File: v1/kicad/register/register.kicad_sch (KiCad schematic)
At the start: 5 parts, among them J1 DBUS, J2 BASE, J3 CTRL, U1 74LS173, U2 74LS173

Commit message: progress on kicad implementation
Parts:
- removed J1: DBUS, Connector_PinSocket_2.54mm:PinSocket_1x08_P2.54mm_Vertical, symbol Connector_Generic:Conn_01x08
- removed J2: BASE, Connector_PinSocket_2.54mm:PinSocket_1x04_P2.54mm_Vertical, symbol Connector_Generic:Conn_01x04
- removed J3: CTRL, Connector_PinHeader_2.54mm:PinHeader_1x03_P2.54mm_Vertical, symbol Connector_Generic:Conn_01x03
- removed U1, U2: 74LS173, Package_DIP:DIP-16_W7.62mm, symbol 74xx:74LS173
- added J1: RegisterSocket (active-high reset), LNCPU:RegisterPort, symbol LNCPU:RegisterSocket (active-high reset)
- added J2: RegisterCtrl, Connector_PinHeader_2.54mm:PinHeader_1x03_P2.54mm_Vertical, symbol LNCPU:RegisterCtrl
- added J3: ASYNC_{out}, Connector_PinSocket_2.54mm:PinSocket_1x08_P2.54mm_Vertical, symbol Connector_Generic:Conn_01x08
- added U1, U2: 74HC173, Package_DIP:DIP-16_W7.62mm_LongPads, symbol 74xx:74HC173
- added U3: 74LS244, Package_DIP:DIP-20_W7.62mm_LongPads, symbol 74xx:74LS244
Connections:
- new net: J1.1 (VCC), U1.16 (VCC), U2.16 (VCC), U3.20 (VCC)
- new net: J1.2 (RST), U1.15 (Mr), U2.15 (Mr)
- new net: J1.3 (CLK), U1.7 (Cp), U2.7 (Cp)
- new net: J1.4 (GND), U1.1 (Oe1), U1.2 (Oe2), U1.8 (GND), U2.1 (Oe1), U2.2 (Oe2), U2.8 (GND), U3.10 (GND)
- new net: J2.1 (~{EN}), U1.10 (E2), U2.10 (E2), U3.1 (OEa)
- new net: J2.2 (~{R_{in}}), U1.9 (E1), U2.9 (E1)
- new net: J2.3 (~{R_{out}}), U3.19 (OEb)
- new net ASYNC0: J3.1 (Pin_1), U1.3 (Q0), U3.2 (I0a)
- new net ASYNC1: J3.2 (Pin_2), U1.4 (Q1), U3.4 (I1a)
- new net ASYNC2: J3.3 (Pin_3), U1.5 (Q2), U3.6 (I2a)
- new net ASYNC3: J3.4 (Pin_4), U1.6 (Q3), U3.8 (I3a)
- new net ASYNC4: J3.5 (Pin_5), U2.3 (Q0), U3.11 (I0b)
- new net ASYNC5: J3.6 (Pin_6), U2.4 (Q1), U3.13 (I1b)
- new net ASYNC6: J3.7 (Pin_7), U2.5 (Q2), U3.15 (I2b)
- new net ASYNC7: J3.8 (Pin_8), U2.6 (Q3), U3.17 (I3b)
- new net DBUS0: J1.5 (DBUS0), U1.14 (D0), U3.18 (O0a)
- new net DBUS1: J1.6 (DBUS1), U1.13 (D1), U3.16 (O1a)
- new net DBUS2: J1.7 (DBUS2), U1.12 (D2), U3.14 (O2a)
- new net DBUS3: J1.8 (DBUS3), U1.11 (D3), U3.12 (O3a)
- new net DBUS4: J1.9 (DBUS4), U2.14 (D0), U3.9 (O0b)
- new net DBUS5: J1.10 (DBUS5), U2.13 (D1), U3.7 (O1b)
- new net DBUS6: J1.11 (DBUS6), U2.12 (D2), U3.5 (O2b)
- new net DBUS7: J1.12 (DBUS7), U2.11 (D3), U3.3 (O3b)

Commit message: feat: update KiCad files with new pin configurations and error handling improvements
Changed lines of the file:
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@@
 (kicad_sch
-	(version 20231120)
+	(version 20250114)
 	(generator "eeschema")
-	(generator_version "8.0")
+	(generator_version "9.0")
 	(paper "A4")
 	(junction
@@
 	(label "ASYNC1"
 		(at 185.42 31.75 0)
-		(fields_autoplaced yes)
 		(effects
 			(font
@@
 	(label "ASYNC7"
 		(at 121.92 36.83 180)
-		(fields_autoplaced yes)
 		(effects
 			(font
@@
 	(label "ASYNC2"
 		(at 185.42 34.29 0)
-		(fields_autoplaced yes)
 		(effects
 			(font
@@
 	(label "ASYNC4"
 		(at 185.42 39.37 0)
-		(fields_autoplaced yes)
 		(effects
 			(font
@@
 	(label "ASYNC5"
 		(at 185.42 41.91 0)
-		(fields_autoplaced yes)
 		(effects
 			(font
@@
 	(label "ASYNC4"
 		(at 151.13 118.11 0)
-		(fields_autoplaced yes)
 		(effects
 			(font
@@
 	(label "ASYNC3"
 		(at 153.67 118.11 0)
-		(fields_autoplaced yes)
 		(effects
 			(font
@@
 	(label "DBUS6"
 		(at 102.87 149.86 0)
-		(fields_autoplaced yes)
 		(effects
 			(font
@@
 	(label "DBUS7"
 		(at 100.33 147.32 0)
-		(fields_autoplaced yes)
 		(effects
 			(font
@@
 	(label "ASYNC0"
 		(at 123.19 92.71 180)
-		(fields_autoplaced yes)
 		(effects
 			(font
@@
 	(label "DBUS4"
 		(at 107.95 154.94 0)
-		(fields_autoplaced yes)
 		(effects
 			(font
@@
 	(label "DBUS7"
 		(at 68.58 36.83 0)
-		(fields_autoplaced yes)
 		(effects
 			(font
@@
 	(label "ASYNC6"
 		(at 121.92 34.29 180)
-		(fields_autoplaced yes)
 		(effects
 			(font
@@
 	(label "DBUS0"
 		(at 210.82 29.21 180)
-		(fields_autoplaced yes)
 		(effects
 			(font
@@
 	(label "DBUS[0..7]"
 		(at 64.77 24.13 0)
-		(fields_autoplaced yes)
 		(effects
 			(font
@@
 	(label "DBUS3"
 		(at 110.49 157.48 0)
-		(fields_autoplaced yes)
 		(effects
 			(font
@@
 	(label "DBUS1"
 		(at 67.31 95.25 0)
-		(fields_autoplaced yes)
 		(effects
 			(font
@@
 	(label "DBUS2"
 		(at 67.31 97.79 0)
-		(fields_autoplaced yes)
 		(effects
 			(font
@@
 	(label "ASYNC0"
 		(at 161.29 118.11 0)
-		(fields_autoplaced yes)
 		(effects
 			(font
@@
 	(label "DBUS3"
 		(at 210.82 36.83 180)
-		(fields_autoplaced yes)
 		(effects
 			(font
@@
 	(label "DBUS0"
 		(at 67.31 92.71 0)
-		(fields_autoplaced yes)
 		(effects
 			(font
@@
 	(label "ASYNC4"
 		(at 121.92 29.21 180)
-		(fields_autoplaced yes)
 		(effects
 			(font
@@
 	(label "DBUS6"
 		(at 68.58 34.29 0)
-		(fields_autoplaced yes)
 		(effects
 			(font
@@
 	(label "ASYNC6"
 		(at 185.42 44.45 0)
-		(fields_autoplaced yes)
 		(effects
 			(font
@@
 	(label "DBUS4"
 		(at 210.82 39.37 180)
-		(fields_autoplaced yes)
 		(effects
 			(font
@@
 	(label "DBUS2"
 		(at 113.03 160.02 0)
-		(fields_autoplaced yes)
 		(effects
 			(font
@@
 	(label "ASYNC[0..7]"
 		(at 125.73 24.13 180)
-		(fields_autoplaced yes)
 		(effects
 			(font
@@
 	(label "ASYNC3"
 		(at 123.19 100.33 180)
-		(fields_autoplaced yes)
 		(effects
 			(font
@@
 	(label "DBUS7"
 		(at 210.82 46.99 180)
-		(fields_autoplaced yes)
 		(effects
 			(font
@@
 	(label "ASYNC5"
 		(at 148.59 118.11 0)
-		(fields_autoplaced yes)
 		(effects
 			(font
@@
 	(label "ASYNC2"
 		(at 123.19 97.79 180)
-		(fields_autoplaced yes)
 		(effects
 			(font
@@
 	(label "DBUS5"
 		(at 68.58 31.75 0)
-		(fields_autoplaced yes)
 		(effects
 			(font
@@
 	(label "ASYNC0"
 		(at 185.42 29.21 0)
-		(fields_autoplaced yes)
 		(effects
 			(font
@@
 	(label "DBUS6"
 		(at 210.82 44.45 180)
-		(fields_autoplaced yes)
 		(effects
 			(font
@@
 	(label "ASYNC1"
 		(at 158.75 118.11 0)
-		(fields_autoplaced yes)
 		(effects
 			(font
@@
 	(label "DBUS1"
 		(at 210.82 31.75 180)
-		(fields_autoplaced yes)
 		(effects
 			(font
@@
 	(label "DBUS0"
 		(at 118.11 165.1 0)
-		(fields_autoplaced yes)
 		(effects
 			(font
@@
 	(label "DBUS3"
 		(at 67.31 100.33 0)
-		(fields_autoplaced yes)
 		(effects
 			(font
@@
 	(label "DBUS5"
 		(at 105.41 152.4 0)
-		(fields_autoplaced yes)
 		(effects
 			(font
@@
 	(label "ASYNC3"
 		(at 185.42 36.83 0)
-		(fields_autoplaced yes)
 		(effects
 			(font
@@
 	(label "DBUS2"
 		(at 210.82 34.29 180)
-		(fields_autoplaced yes)
 		(effects
 			(font
@@
 	(label "ASYNC7"
 		(at 143.51 118.11 0)
-		(fields_autoplaced yes)
 		(effects
 			(font
@@
 	(label "DBUS5"
 		(at 210.82 41.91 180)
-		(fields_autoplaced yes)
 		(effects
 			(font
@@
 	(label "ASYNC6"
 		(at 146.05 118.11 0)
-		(fields_autoplaced yes)
 		(effects
 			(font
@@
 	(label "DBUS1"
 		(at 115.57 162.56 0)
-		(fields_autoplaced yes)
 		(effects
 			(font
@@
 	(label "ASYNC5"
 		(at 121.92 31.75 180)
-		(fields_autoplaced yes)
 		(effects
 			(font
@@
 	(label "DBUS4"
 		(at 68.58 29.21 0)
-		(fields_autoplaced yes)
 		(effects
 			(font
@@
 	(label "ASYNC2"
 		(at 156.21 118.11 0)
-		(fields_autoplaced yes)
 		(effects
 			(font
@@
 	(label "ASYNC7"
 		(at 185.42 46.99 0)
-		(fields_autoplaced yes)
 		(effects
 			(font
@@
 	(label "ASYNC1"
 		(at 123.19 95.25 180)
-		(fields_autoplaced yes)
 		(effects
 			(font
@@
 		)
 		(property "Value" "RegisterSocket (active-high reset)"
-			(at 114.3 172.72 90)
+			(at 115.57 176.276 90)
 			(effects
 				(font
@@
 		)
 	)
+	(embedded_fonts no)
 )

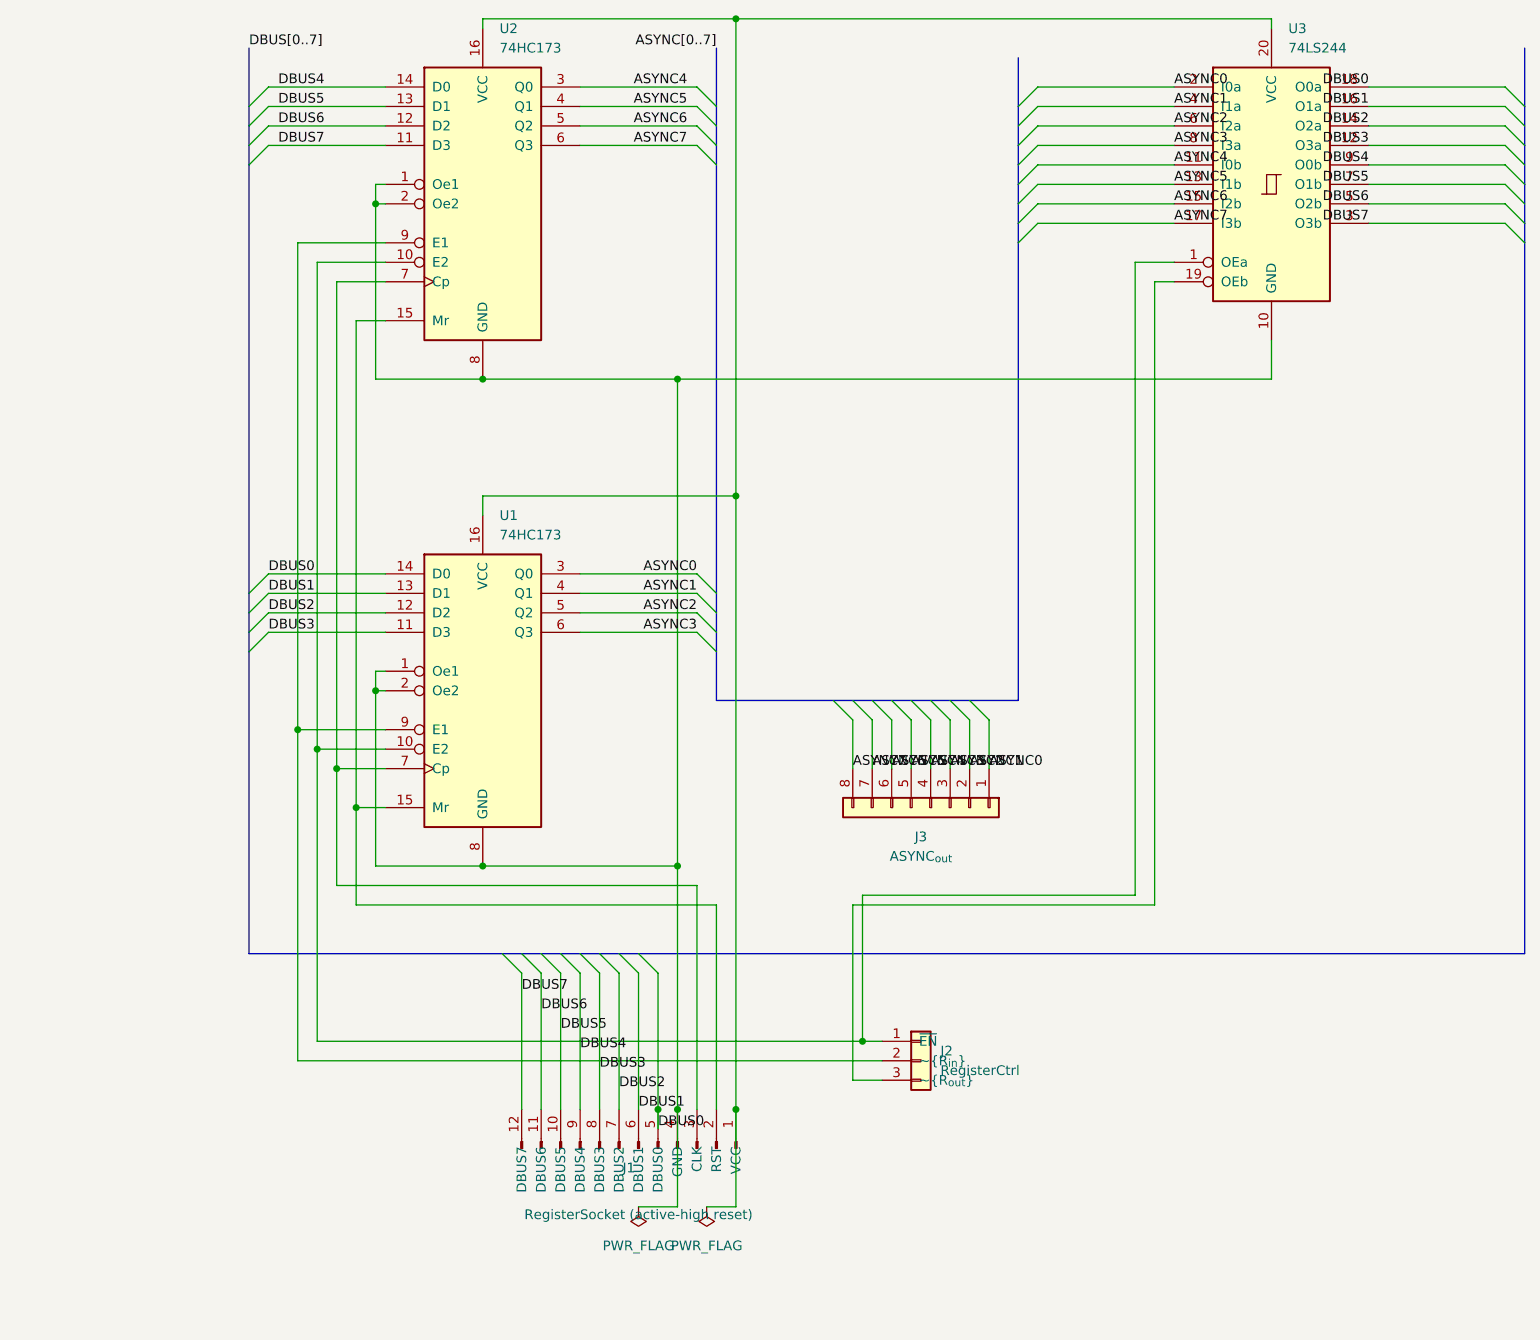
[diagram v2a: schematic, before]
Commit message: add circuits for AT28C64B loader and register, add v1 components library
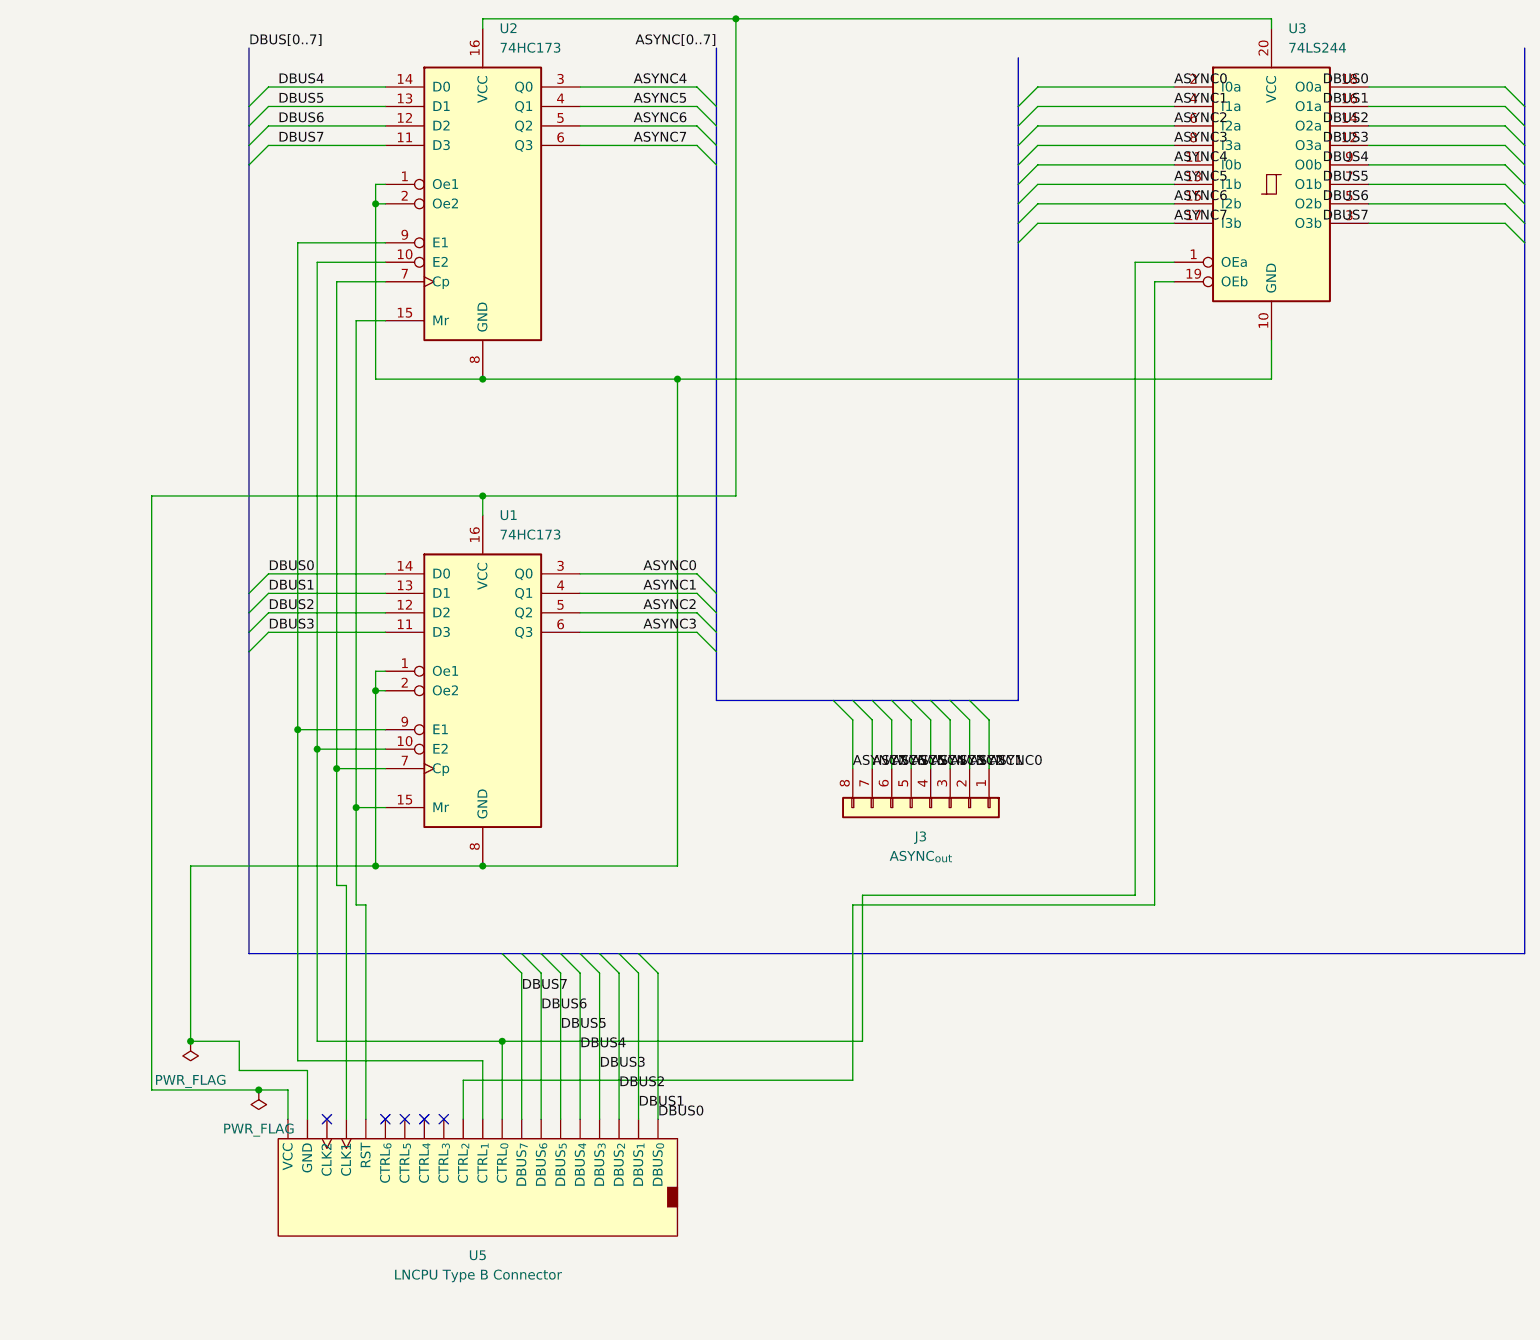
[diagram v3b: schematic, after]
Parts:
- removed J1: RegisterSocket (active-high reset), LNCPU:RegisterPort, symbol LNCPU:RegisterSocket (active-high reset)
- removed J2: RegisterCtrl, Connector_PinHeader_2.54mm:PinHeader_1x03_P2.54mm_Vertical, symbol LNCPU:RegisterCtrl
- added U5: LNCPU Type B Connector, lncpu:LNCPU_Type_B_Header, symbol lncpu:LNCPU_Type_B_Connector
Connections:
- net DBUS0: now also U5.4 (DBUS_{0})
- net DBUS1: now also U5.6 (DBUS_{1})
- net DBUS2: now also U5.8 (DBUS_{2})
- net DBUS3: now also U5.10 (DBUS_{3})
- net DBUS4: now also U5.12 (DBUS_{4})
- net DBUS5: now also U5.14 (DBUS_{5})
- net DBUS6: now also U5.16 (DBUS_{6})
- net DBUS7: now also U5.18 (DBUS_{7})
- net at U1.16 (VCC), U2.16 (VCC), U3.20 (VCC): now also U5.2 (VCC), U5.24 (VCC)
- net at U1.15 (Mr), U2.15 (Mr): now also U5.19 (RST)
- net at U1.7 (Cp), U2.7 (Cp): now also U5.21 (CLK1)
- net at U1.1 (Oe1), U1.2 (Oe2), U1.8 (GND)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: now also U5.1 (GND), U5.17 (GND), U5.20 (GND), U5.22 (GND)
- net at U1.10 (E2), U2.10 (E2), U3.1 (OEa): now also U5.3 (CTRL_{0})
- net at U1.9 (E1), U2.9 (E1): now also U5.5 (CTRL_{1})
- net at U3.19 (OEb): now also U5.7 (CTRL_{2})
- no-connect marks 0 -> 5
